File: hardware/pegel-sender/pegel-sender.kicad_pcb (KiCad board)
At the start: 2 copper layers, 100 x 70 mm, 95 parts, among them J1 SOLAR, J2 AKKU 3,2V, J3 SONDE V+ V- A B, J4 NTC extern, J5 XIAO D0-D6, J6 XIAO 5V-D7, Q1 AOD4189, Q2 FS8205A, Q3 FS8205A, Q4 AO3401A, Q5 2N7002, Q6 2N7002, Q7 SI2318CDS, U1 CN3795, U2 INA226, U3 HY2112-CB, U4 TPS63900, U5 TPS61040, U6 SC16IS740, U7 MAX3485, U8 TLV3402, Y1 14.7456MHz

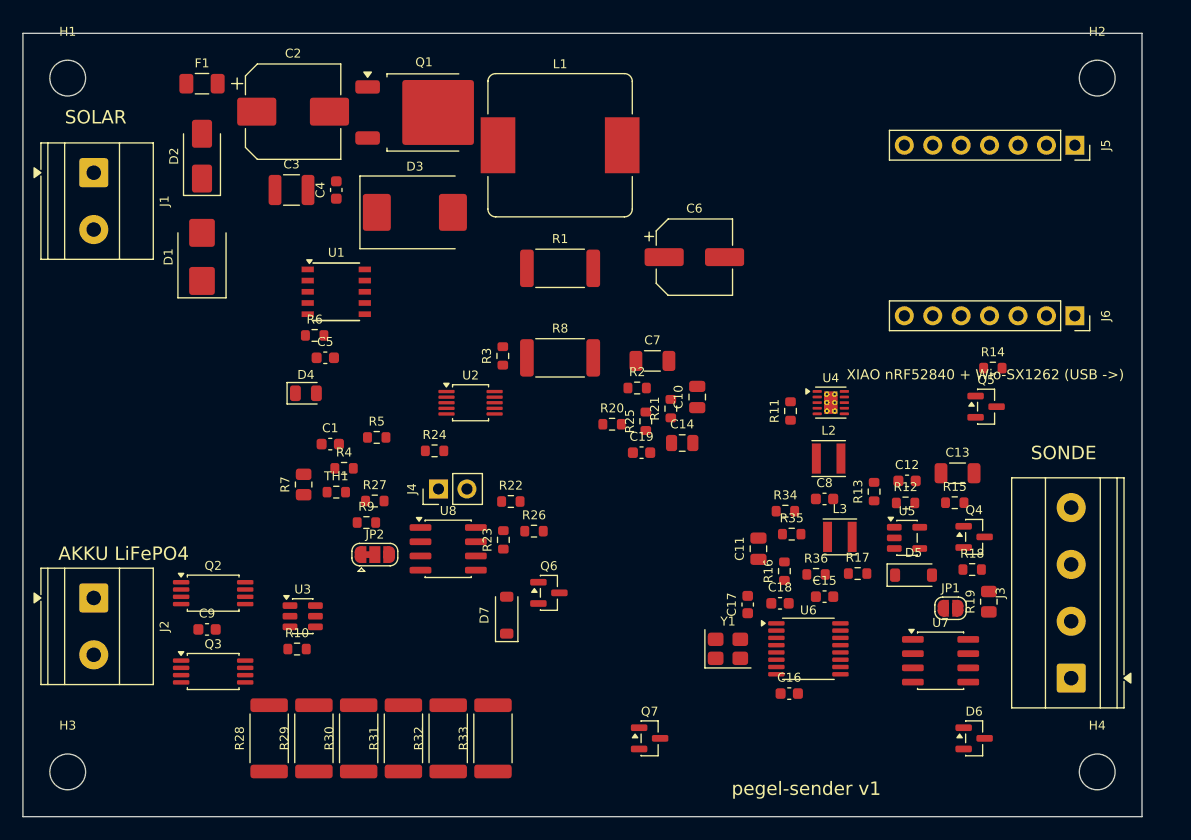
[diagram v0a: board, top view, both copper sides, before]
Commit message: hardware: route carrier board with Freerouting, GND stitching, fab data
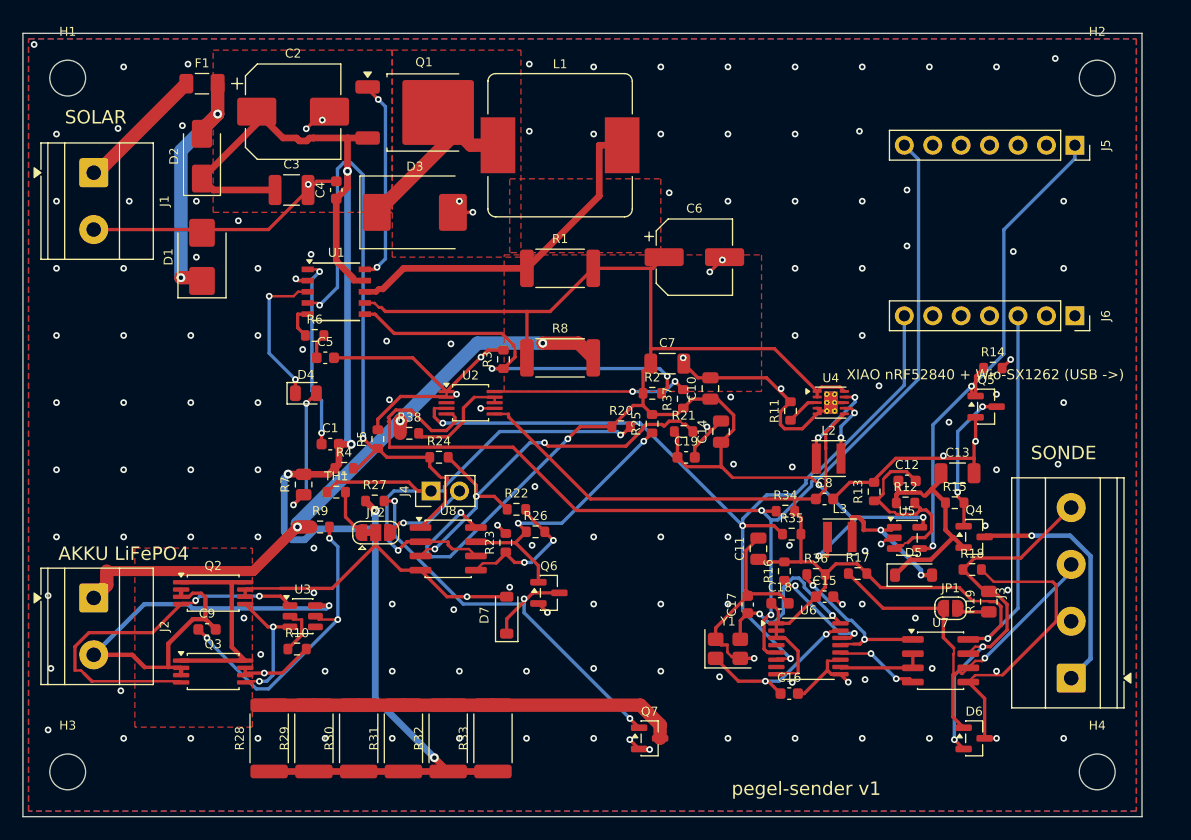
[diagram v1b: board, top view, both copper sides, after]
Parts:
- added R37: 10, Resistor_SMD:R_0603_1608Metric, F.Cu at (109.0, 82.7)
- added R38: 10, Resistor_SMD:R_0603_1608Metric, F.Cu at (84.5, 85.7)
- moved R9 4.15 mm to (76.6, 94.1)
- moved C19 4.01 mm to (109.3, 87.9)
- moved C14 3.61 mm to (112.4, 85.6), turned to 90 degrees
- moved R21 2.34 mm to (109.0, 85.6), turned to 0 degrees
- moved JP2 1.97 mm to (81.5, 94.6)
- moved R2 1.44 mm to (106.2, 82.2)
- moved C10 1.41 mm to (111.4, 81.7)
- moved C7 1.35 mm to (107.6, 79.5)
- moved R22 0.86 mm to (94.1, 92.5)
- moved R20 0.84 mm to (103.5, 85.2)
- moved R24 0.70 mm to (87.2, 87.9)
- moved J4 0.69 mm to (86.5, 90.9)
- moved R25 0.60 mm to (106.2, 84.9)
- moved R23 0.33 mm to (93.1, 95.5)
- moved R3 0.31 mm to (92.9, 79.1)
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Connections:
- U2 pad 10: VSYS -> INA_P
- U2 pad 8: BAT_P -> INA_M
- U2 pad 9: BAT_P -> INA_M
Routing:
- net GND: track 0.00 -> 201.1 mm, vias 0 -> 149
- net VSYS: track 0.00 -> 146.7 mm, vias 0 -> 5
- net VSOL: track 0.00 -> 134.3 mm, vias 0 -> 5
- net +3V3: track 0.00 -> 122.5 mm, vias 0 -> 1
- net I2C_SCL: track 0.00 -> 102.7 mm, vias 0 -> 2
- net I2C_SDA: track 0.00 -> 78.7 mm, vias 0 -> 3
- net MPPT: track 0.00 -> 58.4 mm, vias 0 -> 2
- net BAT_P: track 0.00 -> 57.9 mm, vias 0 -> 3
- net T_NTC: track 0.00 -> 47.9 mm, vias 0 -> 2
- net SENS_EN: track 0.00 -> 46.2 mm, vias 0 -> 2
- net BAT_N: track 0.00 -> 46.1 mm, vias 0 -> 1
- net HEAT_G: track 0.00 -> 41.1 mm, vias 0 -> 3
- net T_REF0: track 0.00 -> 38.5 mm, vias 0 -> 3
- net HEAT_N: track 0.00 -> 36.9 mm
- net RS485_A: track 0.00 -> 36.6 mm, vias 0 -> 1
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- added copper zone on F.Cu, net BAT_N
- added copper zone on F.Cu, net CHG_CSP
- added copper zone on F.Cu, net CHG_SW
- added copper zone on B.Cu, net GND
- added copper zone on F.Cu, net GND
- added copper zone on F.Cu, net VSOL
- added copper zone on F.Cu, net VSYS

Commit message: Board silkscreen labels, sender firmware for the carrier board
- Connector pin labels (solar/battery +/-, probe wire colors), jumper values on silkscreen
- SC16IS740 I2C UART driver with automatic RS485 direction, INA226 battery readout
- Probe supply on D0 switched on ahead of each measurement (PEGEL_SENSOR_WARMUP_MS)
- PEGEL_BOARD selects carrier board (default) or the RS485-module breadboard setup
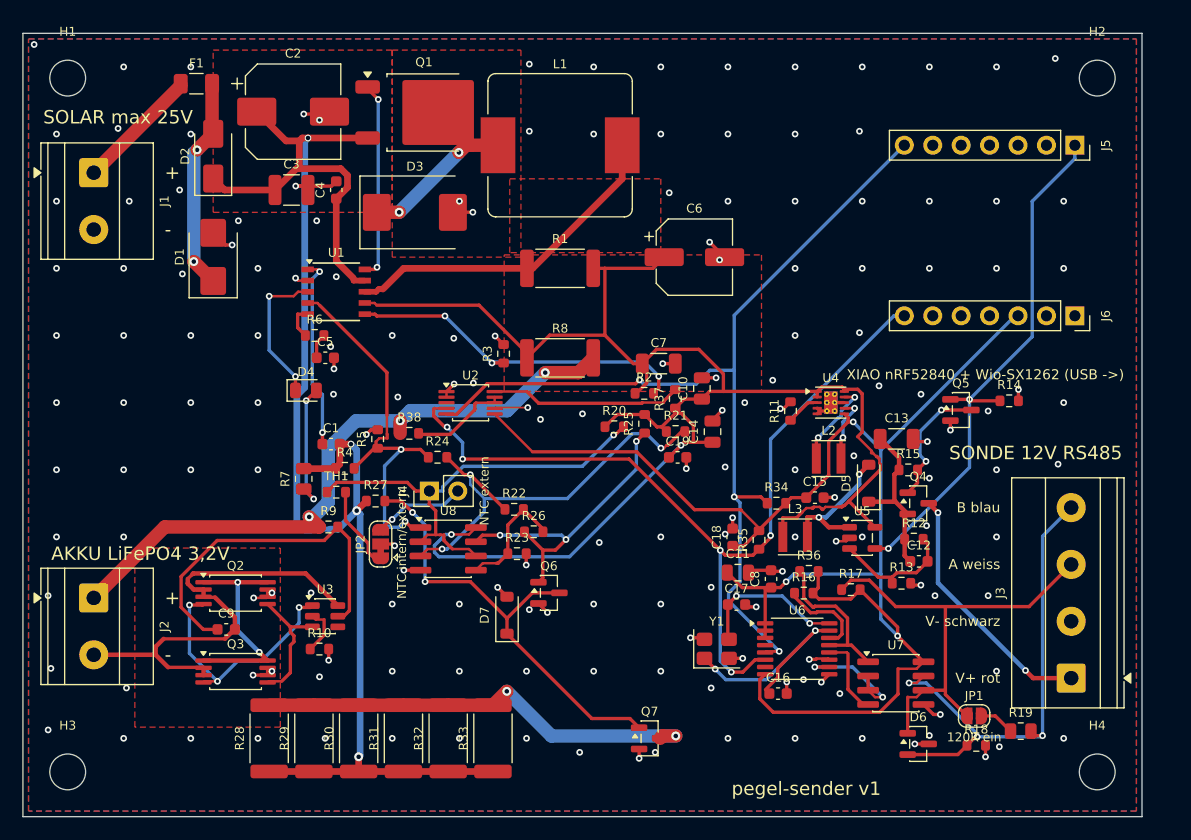
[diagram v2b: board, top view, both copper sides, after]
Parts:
- moved R18 15.7 mm to (135.2, 113.6)
- moved R19 11.9 mm to (139.2, 112.4), turned to 0 degrees
- moved JP1 9.85 mm to (135.0, 111.0)
- moved D5 9.14 mm to (125.6, 90.2), turned to 90 degrees
- moved C15 8.89 mm to (120.8, 91.5)
- moved C8 8.60 mm to (116.9, 98.8), turned to 90 degrees
- moved R13 8.54 mm to (128.5, 99.1), turned to 0 degrees
- moved C12 7.27 mm to (130.1, 97.2)
- moved C18 7.27 mm to (113.4, 95.0), turned to 90 degrees
- moved C13 6.25 mm to (128.1, 86.2)
- moved Q4 5.83 mm to (130.0, 92.0)
- moved R15 5.08 mm to (129.1, 89.0)
- moved D6 5.02 mm to (130.0, 113.5)
- moved U7 4.47 mm to (128.0, 108.1)
- moved L3 4.00 mm to (119.0, 95.0)
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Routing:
- net GND: track 201.1 -> 64.3 mm, vias 149 -> 171
- net MPPT: track 58.4 -> 36.0 mm
- net +3V3: track 122.5 -> 139.7 mm, vias 1 -> 3
- net I2C_SCL: track 102.7 -> 86.2 mm, vias 2 -> 3
- net PROT_OD: track 33.6 -> 22.5 mm, vias 2 -> 3
- net RS485_B: track 34.4 -> 45.2 mm, vias 2 -> 3
- net T_NTC: track 47.9 -> 40.2 mm, vias 2 -> 1
- net BST_FB: track 17.9 -> 11.3 mm
- net XTAL1: track 15.7 -> 21.4 mm
- net V12_RAW: track 20.2 -> 15.0 mm
- net BAT_N: track 46.1 -> 41.5 mm, vias 1 -> 0
- net CHG_FB: track 35.7 -> 31.4 mm, vias 2 -> 3
- net RS485_A: track 36.6 -> 40.8 mm, vias 1 -> 0
- net SOLAR_F: track 23.0 -> 19.1 mm
- net PROT_VDD: track 28.0 -> 31.8 mm, vias 3 -> 0
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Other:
- board text added: "+"
- board text added: "-"
- board text added: "A weiss"
- board text added: "AKKU LiFePO4 3,2V"
- board text added: "B blau"
- board text added: "SOLAR max 25V"
- board text added: "SONDE 12V RS485"
- board text added: "V+ rot"
- board text added: "V- schwarz"
- board text removed: "AKKU LiFePO4"
- board text removed: "SOLAR"
- board text removed: "SONDE"

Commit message: hardware: publish wired schematics and fab
Block PNGs stay in git so the README renders. Ignore ERC
reports, accidental plots, and KiCad backups. Drop stale
fab board previews. Sender skips the probe when the pack
is low.
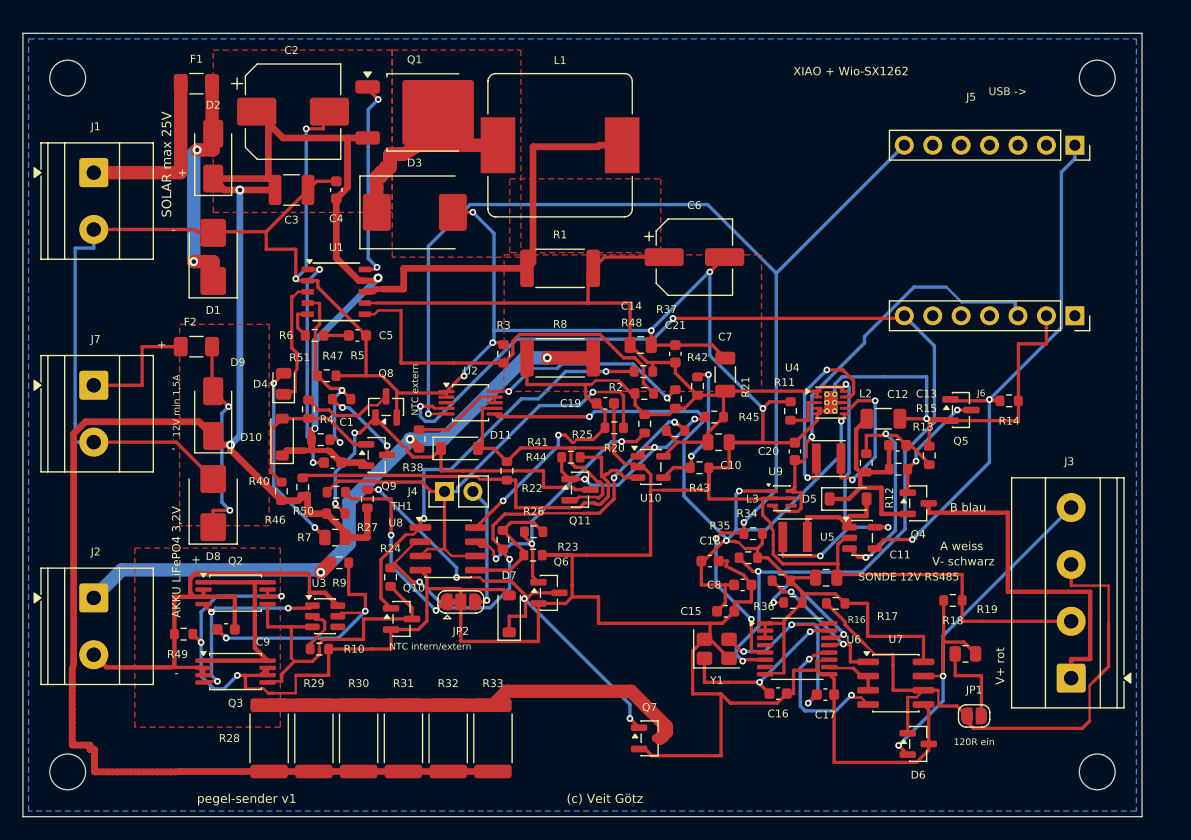
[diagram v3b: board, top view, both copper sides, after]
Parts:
- added C20: 1uF, Capacitor_SMD:C_0603_1608Metric, F.Cu at (119.0, 87.4)
- added C21: 100nF, Capacitor_SMD:C_0603_1608Metric, F.Cu at (108.3, 78.6)
- added D10: 10V, Diode_SMD:D_SOD-123, F.Cu at (73.2, 86.1)
- added D11: 10V, Diode_SMD:D_SOD-123, F.Cu at (89.0, 87.1)
- added D8: SMBJ18A, Diode_SMD:D_SMB, F.Cu at (67.0, 92.0)
- added D9: SS34, Diode_SMD:D_SMA, F.Cu at (67.0, 84.0)
- added F2: 2A, Fuse:Fuse_1206_3216Metric, F.Cu at (65.5, 78.0)
- added J7: 12V, TerminalBlock_Phoenix:TerminalBlock_Phoenix_MKDS-1,5-2-5.08_1x02_P5.08mm_Horizontal, F.Cu at (56.3, 81.5)
- added Q10: 2N7002, Package_TO_SOT_SMD:SOT-23, F.Cu at (83.8, 102.3)
- added Q11: 2N7002, Package_TO_SOT_SMD:SOT-23, F.Cu at (99.8, 90.8)
- added Q8: 2N7002, Package_TO_SOT_SMD:SOT-23, F.Cu at (82.5, 83.4)
- added Q9: AO3401A, Package_TO_SOT_SMD:SOT-23, F.Cu at (81.6, 87.7)
- added R40: 470k, Resistor_SMD:R_0603_1608Metric, F.Cu at (75.0, 90.5)
- added R41: 68.1k, Resistor_SMD:R_0603_1608Metric, F.Cu at (93.2, 89.1)
- added R42: 97.6k, Resistor_SMD:R_0603_1608Metric, F.Cu at (110.3, 81.5)
- added R43: 100k, Resistor_SMD:R_0603_1608Metric, F.Cu at (110.5, 88.8)
- added R44: 1M, Resistor_SMD:R_0603_1608Metric, F.Cu at (99.0, 87.9)
- added R45: 1M, Resistor_SMD:R_0603_1608Metric, F.Cu at (111.8, 84.3)
- added R46: 100k, Resistor_SMD:R_0603_1608Metric, F.Cu at (73.1, 90.9)
- added R47: 330k, Resistor_SMD:R_0603_1608Metric, F.Cu at (78.5, 82.7)
- added R48: 1M, Resistor_SMD:R_0603_1608Metric, F.Cu at (105.5, 80.2)
- added R49: 100k, Resistor_SMD:R_0603_1608Metric, F.Cu at (64.4, 103.7)
- added R50: 1M, Resistor_SMD:R_0603_1608Metric, F.Cu at (78.0, 92.9)
- added R51: 10k, Resistor_SMD:R_0603_1608Metric, F.Cu at (75.5, 83.6)
- added U10: TLV3401, Package_TO_SOT_SMD:SOT-23-5, F.Cu at (106.1, 88.8)
- added U9: LM66100, Package_TO_SOT_SMD:SOT-363_SC-70-6, F.Cu at (117.8, 91.5)
- C16, C17: value 18pF -> 27pF
- R21: value 499k -> 470k
- R22: value 26.1k -> 28.7k
- R23: value 475k -> 499k
- TH1: value 100k B3950 -> 100k B4250
- moved R18 13.1 mm to (133.1, 100.7)
- moved C15 12.9 mm to (112.8, 101.7)
- moved R13 11.7 mm to (131.0, 87.7), turned to 90 degrees
- moved R24 11.5 mm to (82.8, 98.6), turned to 90 degrees
- moved C17 11.3 mm to (121.7, 109.1)
- moved C12 10.5 mm to (128.2, 86.8)
- moved C14 10.1 mm to (105.2, 77.8), turned to 0 degrees
- moved JP2 8.84 mm to (89.1, 100.8), turned to 0 degrees
- moved R19 8.49 mm to (134.2, 105.5)
- moved C19 8.06 mm to (102.0, 83.1)
- moved R12 8.03 mm to (125.4, 88.4), turned to 90 degrees
- moved C11 7.91 mm to (121.8, 98.7)
- moved R5 7.26 mm to (77.2, 80.6), turned to 0 degrees
- moved C7 6.03 mm to (112.8, 80.5), turned to 90 degrees
- moved R7 5.95 mm to (77.9, 95.1), turned to 0 degrees
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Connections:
- J6 pad 3: +3V3 -> XIAO_3V3
- R24 pad 1: MPPT -> PROT_OC
- U8 pad 1: MPPT -> CHG_INHIBIT
- U8 pad 2: T_NTC -> T_REF0
- U8 pad 3: T_REF0 -> T_NTC
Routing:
- net GND: track 64.3 -> 526.7 mm, vias 171 -> 12
- net VSOL: track 136.7 -> 195.5 mm
- net VSOL_DIV: track 0.00 -> 39.9 mm
- net XIAO_3V3: track 0.00 -> 39.5 mm, vias 0 -> 1
- net CHG_INHIBIT: track 0.00 -> 37.2 mm, vias 0 -> 2
- net MPPT_NG: track 0.00 -> 35.5 mm, vias 0 -> 2
- net +3V3: track 139.7 -> 109.0 mm, vias 3 -> 4
- net I2C_SCL: track 86.2 -> 107.8 mm, vias 3 -> 4
- net I2C_SDA: track 78.7 -> 100.0 mm, vias 5 -> 4
- net MPPT_EN: track 0.00 -> 19.0 mm, vias 0 -> 3
- net DC_F: track 0.00 -> 18.8 mm, vias 0 -> 2
- net PROT_OC: track 11.6 -> 30.2 mm
- net MPPT: track 36.0 -> 17.8 mm
- net MPPT_GATE: track 0.00 -> 14.9 mm
- net RS485_A: track 40.8 -> 54.4 mm
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- added copper zone on F.Cu, net DC_F
- removed copper zone on F.Cu, net GND
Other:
- board text added: "(c) Veit Götz"
- board text added: "12V min 1,5A"
- board text added: "USB ->"
- board text added: "XIAO + Wio-SX1262"
- board text removed: "XIAO nRF52840 + Wio-SX1262 (USB ->)"

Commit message: hardware: fix frost lockout, Q4 gate overvoltage, MPPT threshold reference
- Frost lockout pulls the CN3795 MPPT pin again instead of the protection's charge FET:
  with that FET off, its body diode sits in the discharge path and ~0.6 V across the
  FETs trips the HY2112 discharge overcurrent (100-200 mV), disconnecting the battery
- Hysteresis from the comparator output to T_NTC (4.7M, ~1 K)
- Q4 (AO3401A, Vgs max 12 V) saw -12.3 V; R53 divides to -6.2 V
- MPPT/12 V-supply threshold referenced to +3V3 instead of VSYS (was 11.2 V at a
  2.8 V battery, so a 12 V supply could not charge an empty battery); 976k/1M
- SMAJ15A on the probe supply line, CHRG LED resistor 10k (0.11 W at 25 V in 0805)
- kicad_env/schematic_wired: find KiCad on Windows, single-file symbol libs,
  rsvg-convert optional
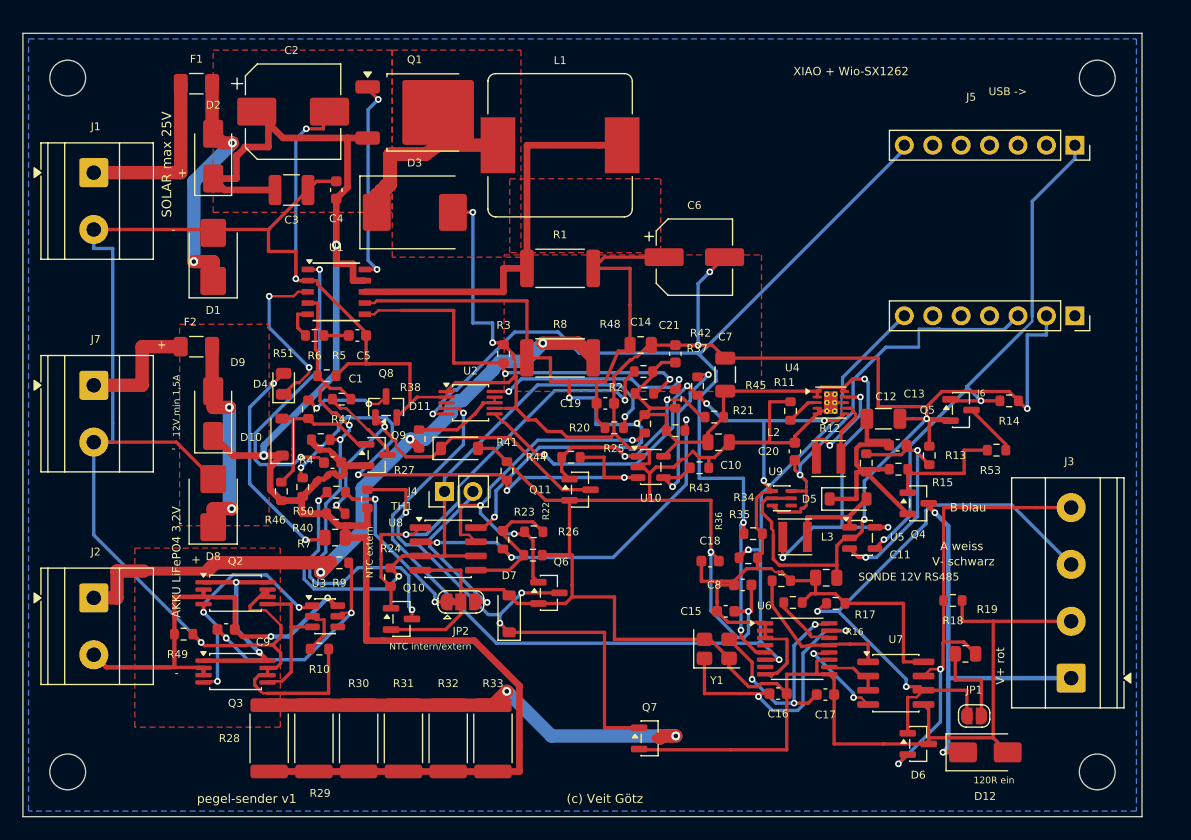
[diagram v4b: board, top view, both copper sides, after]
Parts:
- added D12: SMAJ15A, Diode_SMD:D_SMA, F.Cu at (136.0, 114.2)
- added R53: 100k, Resistor_SMD:R_0603_1608Metric, F.Cu at (137.0, 87.2)
- R24: value 10M -> 4.7M
- R42: value 97.6k -> 976k
- R43: value 100k -> 1M
- R7: value 4.7k -> 10k
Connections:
- Q10 pad 3: PROT_OC -> MPPT
- Q5 pad 3: PSW_G -> PSW_PD
- R24 pad 1: PROT_OC -> CHG_INHIBIT
- R24 pad 2: T_REF0 -> T_NTC
- R42 pad 1: VSYS -> +3V3
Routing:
- net VSOL: track 195.5 -> 155.9 mm, vias 4 -> 2
- net MPPT: track 17.8 -> 46.5 mm, vias 2 -> 3
- net I2C_SCL: track 107.8 -> 89.6 mm, vias 4 -> 3
- net GND: track 526.7 -> 544.8 mm
- net PROT_OC: track 30.2 -> 12.6 mm
- net T_NTC: track 44.8 -> 57.8 mm, vias 1 -> 3
- net VSYS: track 140.4 -> 153.1 mm, vias 5 -> 6
- net T_REF0: track 45.0 -> 34.9 mm, vias 4 -> 3
- net VSOL_DIV: track 39.9 -> 49.7 mm, vias 0 -> 4
- net XTAL1: track 16.6 -> 24.7 mm
- net BB_LX2: track 13.7 -> 5.81 mm, vias 2 -> 0
- net BB_LX1: track 17.9 -> 10.0 mm
- net HEAT_OFF: track 26.9 -> 34.3 mm
- net I2C_SDA: track 100.0 -> 92.7 mm, vias 4 -> 3
- net CHG_VG: track 20.0 -> 27.2 mm
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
